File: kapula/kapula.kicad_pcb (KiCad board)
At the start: 4 copper layers, 50 x 59 mm, 163 parts, among them J1 Conn_02x10_Odd_Even, J12 U.FL, J13 U.FL, J3 Conn_02x10_Odd_Even, J4 Conn_ARM_JTAG_SWD_10, J5 U.FL, J9 U.FL, Q1 AO3401A, Q2 AO3401A, Q3 AO3400A, Q4 BSS84, Q5 AO3400A, Q6 AO3400A, T1 BW21S7511A01TF, T2 BW21S7511A01TF, T3 BW21S7511A01TF, T4 BW21S7511A01TF, U1 XC6206P332MR, U2 TP4054, U3 DW01+G, U5 EFR32FG14P233F256GM48-B, U6 XA213-G4J, X1 DSB221SDN, Y1 32768 Hz

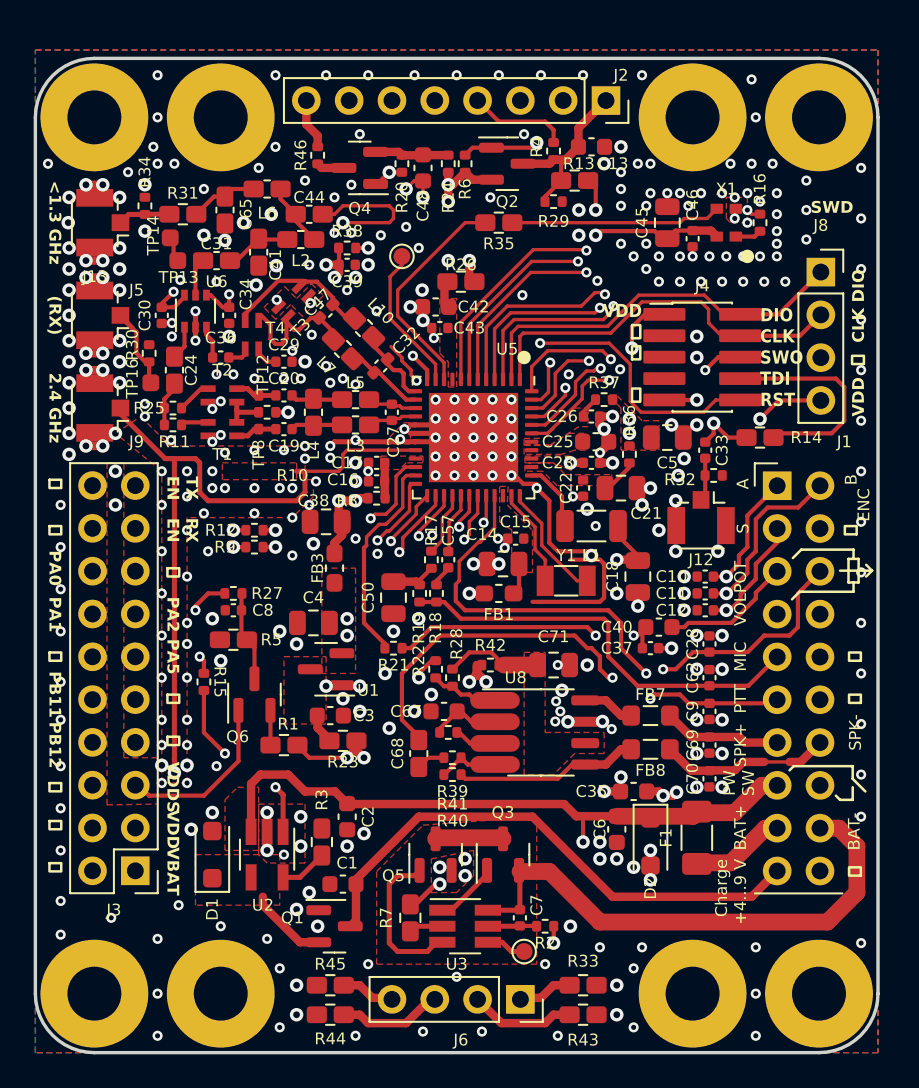
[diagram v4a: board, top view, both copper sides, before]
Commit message: PCB: Add tooling holes
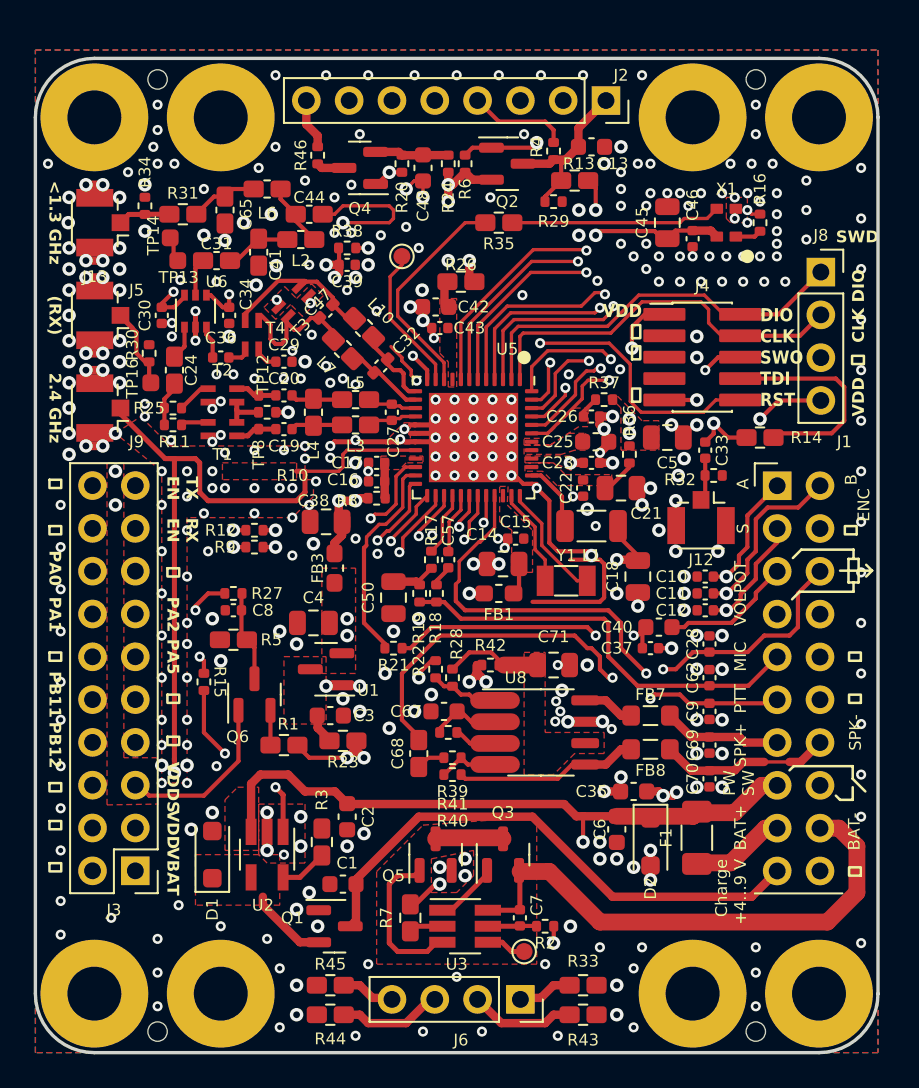
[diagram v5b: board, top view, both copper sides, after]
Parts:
- added H10: ~, kapula:ToolingHole, F.Cu at (142.8, 58.8)
- added H11: ~, kapula:ToolingHole, F.Cu at (107.2, 115.2)
- added H12: ~, kapula:ToolingHole, F.Cu at (142.8, 115.2)
- added H9: ~, kapula:ToolingHole, F.Cu at (107.2, 58.8)
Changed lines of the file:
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@@
     (property "ki_keywords" "connector")
     (attr through_hole)
-    (fp_text reference "J8" (at 0 -2.77 unlocked) (layer "F.SilkS")
+    (fp_text reference "J8" (at 0 -2.18 unlocked) (layer "F.SilkS")
         (effects (font (size 0.7 0.7) (thickness 0.15)))
     )
@@
       (net 82 "Net-(C20-Pad1)") (pinfunction "1") (pintype "passive"))
   )
+  (footprint "kapula:ToolingHole" (layer "F.Cu")
+    (at 142.75 58.75)
+    (property "Sheetfile" "kapula.kicad_sch")
+    (property "Sheetname" "")
+    (property "ki_description" "Mounting Hole without connection")
+    (property "ki_keywords" "mounting hole")
+    (attr through_hole)
+    (fp_text reference "H10" (at 0 0.5) (layer "F.SilkS") hide
+        (effects (font (size 1 1) (thickness 0.15)))
+    )
+    (fp_text value "~" (at 0 -0.5) (layer "F.Fab")
+        (effects (font (size 1 1) (thickness 0.15)))
+    )
+    (pad "" np_thru_hole circle (at 0 0) (size 1.752 1.752) (drill 1.152) (layers "*.Mask")
+      (solder_mask_margin 0.3) (clearance 0.3) (zone_connect 0))
+  )
   (footprint "kapula:R_0402_to_0603_HandSolder" (layer "F.Cu")
     (at 143 80)
@@
     )
   )
+  (footprint "kapula:ToolingHole" (layer "F.Cu")
+    (at 107.25 58.75)
+    (property "Sheetfile" "kapula.kicad_sch")
+    (property "Sheetname" "")
+    (property "ki_description" "Mounting Hole without connection")
+    (property "ki_keywords" "mounting hole")
+    (attr through_hole)
+    (fp_text reference "H9" (at 0 0.5) (layer "F.SilkS") hide
+        (effects (font (size 1 1) (thickness 0.15)))
+    )
+    (fp_text value "~" (at 0 -0.5) (layer "F.Fab")
+        (effects (font (size 1 1) (thickness 0.15)))
+    )
+    (pad "" np_thru_hole circle (at 0 0) (size 1.752 1.752) (drill 1.152) (layers "*.Mask")
+      (solder_mask_margin 0.3) (clearance 0.3) (zone_connect 0))
+  )
   (footprint "Resistor_SMD:R_0402_1005Metric" (layer "F.Cu")
     (at 130.75 66 180)
@@
     )
   )
+  (footprint "kapula:ToolingHole" (layer "F.Cu")
+    (at 107.25 115.25)
+    (property "Sheetfile" "kapula.kicad_sch")
+    (property "Sheetname" "")
+    (property "ki_description" "Mounting Hole without connection")
+    (property "ki_keywords" "mounting hole")
+    (attr through_hole)
+    (fp_text reference "H11" (at 0 0.5) (layer "F.SilkS") hide
+        (effects (font (size 1 1) (thickness 0.15)))
+    )
+    (fp_text value "~" (at 0 -0.5) (layer "F.Fab")
+        (effects (font (size 1 1) (thickness 0.15)))
+    )
+    (pad "" np_thru_hole circle (at 0 0) (size 1.752 1.752) (drill 1.152) (layers "*.Mask")
+      (solder_mask_margin 0.3) (clearance 0.3) (zone_connect 0))
+  )
   (footprint "Connector_PinHeader_2.54mm:PinHeader_2x10_P2.54mm_Vertical" (layer "F.Cu")
     (at 144.02 82.86)
@@
       (net 83 "Net-(C29-Pad2)") (pinfunction "4") (pintype "passive"))
   )
+  (footprint "kapula:ToolingHole" (layer "F.Cu")
+    (at 142.75 115.25)
+    (property "Sheetfile" "kapula.kicad_sch")
+    (property "Sheetname" "")
+    (property "ki_description" "Mounting Hole without connection")
+    (property "ki_keywords" "mounting hole")
+    (attr through_hole)
+    (fp_text reference "H12" (at 0 0.5) (layer "F.SilkS") hide
+        (effects (font (size 1 1) (thickness 0.15)))
+    )
+    (fp_text value "~" (at 0 -0.5) (layer "F.Fab")
+        (effects (font (size 1 1) (thickness 0.15)))
+    )
+    (pad "" np_thru_hole circle (at 0 0) (size 1.752 1.752) (drill 1.152) (layers "*.Mask")
+      (solder_mask_margin 0.3) (clearance 0.3) (zone_connect 0))
+  )
   (footprint "Resistor_SMD:R_0402_1005Metric" (layer "F.Cu")
     (at 133.75 77.75 180)
@@
     (effects (font (size 0.7 0.7) (thickness 0.15)) (justify right bottom mirror))
   )
-  (gr_text "SWD" (at 146 66.75) (layer "F.SilkS")
+  (gr_text "SWD" (at 147.5 68.5) (layer "F.SilkS")
     (effects (font (size 0.7 0.7) (thickness 0.15) bold) (justify left bottom))
   )
@@
   (via (at 138.5 81.25) (size 0.8) (drill 0.4) (layers "F.Cu" "B.Cu") (free) (net 2))
   (via (at 134.25 78.75) (size 0.8) (drill 0.4) (layers "F.Cu" "B.Cu") (net 2))
-  (via (at 107.25 58.5) (size 0.6) (drill 0.3) (layers "F.Cu" "B.Cu") (free) (net 2))
+  (via (at 107.25 60.25) (size 0.6) (drill 0.3) (layers "F.Cu" "B.Cu") (free) (net 2))
   (via (at 149 67) (size 0.6) (drill 0.3) (layers "F.Cu" "B.Cu") (free) (net 2))
   (via (at 105 74.25) (size 0.8) (drill 0.4) (layers "F.Cu" "B.Cu") (free) (net 2))
@@
   (via (at 142.5 63.75) (size 0.6) (drill 0.3) (layers "F.Cu" "B.Cu") (free) (net 2))
   (via (at 119.5 103.5) (size 0.8) (drill 0.4) (layers "F.Cu" "B.Cu") (free) (net 2))
+  (via (at 142.75 111.75) (size 0.6) (drill 0.3) (layers "F.Cu" "B.Cu") (free) (net 2))
   (via (at 106.5 78.75) (size 0.6) (drill 0.3) (layers "F.Cu" "B.Cu") (free) (net 2))
   (via (at 102 78.25) (size 0.8) (drill 0.4) (layers "F.Cu" "B.Cu") (free) (net 2))
@@
   (via (at 125 112) (size 0.6) (drill 0.3) (layers "F.Cu" "B.Cu") (free) (net 2))
   (via (at 104 75) (size 0.8) (drill 0.4) (layers "F.Cu" "B.Cu") (free) (net 2))
-  (via (at 142.75 115.5) (size 0.6) (drill 0.3) (layers "F.Cu" "B.Cu") (free) (net 2))
   (via (at 118.75 65) (size 0.6) (drill 0.3) (layers "F.Cu" "B.Cu") (free) (net 2))
   (via (at 124 106.5) (size 0.8) (drill 0.4) (layers "F.Cu" "B.Cu") (net 2))
@@
   (via (at 122 67.5) (size 0.6) (drill 0.3) (layers "F.Cu" "B.Cu") (free) (net 2))
   (via (at 123.55 85.8) (size 0.6) (drill 0.3) (layers "F.Cu" "B.Cu") (free) (net 2))
-  (via (at 107.25 113) (size 0.6) (drill 0.3) (layers "F.Cu" "B.Cu") (free) (net 2))
+  (via (at 107.25 111.75) (size 0.6) (drill 0.3) (layers "F.Cu" "B.Cu") (free) (net 2))
   (via (at 117.75 67.85) (size 0.6) (drill 0.3) (layers "F.Cu" "B.Cu") (free) (net 2))
   (via (at 140.75 70.75) (size 0.6) (drill 0.3) (layers "F.Cu" "B.Cu") (free) (net 2))
@@
   (via (at 119.75 58.5) (size 0.6) (drill 0.3) (layers "F.Cu" "B.Cu") (net 2))
   (via (at 139.25 100.75) (size 0.8) (drill 0.4) (layers "F.Cu" "B.Cu") (free) (net 2))
-  (via (at 107.25 61) (size 0.6) (drill 0.3) (layers "F.Cu" "B.Cu") (free) (net 2))
+  (via (at 107.25 61.75) (size 0.6) (drill 0.3) (layers "F.Cu" "B.Cu") (free) (net 2))
   (via (at 117.25 94.75) (size 0.8) (drill 0.4) (layers "F.Cu" "B.Cu") (free) (net 2))
   (via (at 127.125 77.75) (size 0.6) (drill 0.3) (layers "F.Cu" "B.Cu") (net 2))
@@
   (via (at 109 96.75) (size 0.6) (drill 0.3) (layers "F.Cu" "B.Cu") (free) (net 2))
   (via (at 138.25 70.75) (size 0.6) (drill 0.3) (layers "F.Cu" "B.Cu") (free) (net 2))
-  (via (at 142.75 61) (size 0.6) (drill 0.3) (layers "F.Cu" "B.Cu") (free) (net 2))
+  (via (at 142.75 62) (size 0.6) (drill 0.3) (layers "F.Cu" "B.Cu") (free) (net 2))
   (via (at 125.5 105) (size 0.8) (drill 0.4) (layers "F.Cu" "B.Cu") (net 2))
   (via (at 124.875 82.25) (size 0.6) (drill 0.3) (layers "F.Cu" "B.Cu") (net 2))
@@
   (via (at 149 110) (size 0.6) (drill 0.3) (layers "F.Cu" "B.Cu") (free) (net 2))
   (via (at 102 75.5) (size 0.8) (drill 0.4) (layers "F.Cu" "B.Cu") (free) (net 2))
-  (via (at 142.75 113) (size 0.6) (drill 0.3) (layers "F.Cu" "B.Cu") (free) (net 2))
+  (via (at 142.75 113.75) (size 0.6) (drill 0.3) (layers "F.Cu" "B.Cu") (free) (net 2))
   (via (at 143.75 63.75) (size 0.6) (drill 0.3) (layers "F.Cu" "B.Cu") (free) (net 2))
   (via (at 119 76.85) (size 0.6) (drill 0.3) (layers "F.Cu" "B.Cu") (free) (net 2))
@@
   (via (at 105 70) (size 0.8) (drill 0.4) (layers "F.Cu" "B.Cu") (free) (net 2))
   (via (at 102 72.75) (size 0.8) (drill 0.4) (layers "F.Cu" "B.Cu") (free) (net 2))
-  (via (at 142.5 58.75) (size 0.6) (drill 0.3) (layers "F.Cu" "B.Cu") (free) (net 2))
+  (via (at 142.75 60.25) (size 0.6) (drill 0.3) (layers "F.Cu" "B.Cu") (free) (net 2))
   (via (at 139.25 79.25) (size 0.8) (drill 0.4) (layers "F.Cu" "B.Cu") (free) (net 2))
   (via (at 136.5 106.25) (size 0.8) (drill 0.4) (layers "F.Cu" "B.Cu") (free) (net 2))
@@
   (via (at 102 65.75) (size 0.8) (drill 0.4) (layers "F.Cu" "B.Cu") (free) (net 2))
   (via (at 142.25 67.25) (size 0.6) (drill 0.3) (layers "F.Cu" "B.Cu") (free) (net 2))
-  (via (at 107.25 115.5) (size 0.6) (drill 0.3) (layers "F.Cu" "B.Cu") (free) (net 2))
+  (via (at 107.25 113.75) (size 0.6) (drill 0.3) (layers "F.Cu" "B.Cu") (free) (net 2))
   (via (at 143 66) (size 0.6) (drill 0.3) (layers "F.Cu" "B.Cu") (free) (net 2))
   (via (at 142.25 66.5) (size 0.6) (drill 0.3) (layers "F.Cu" "B.Cu") (free) (net 2))

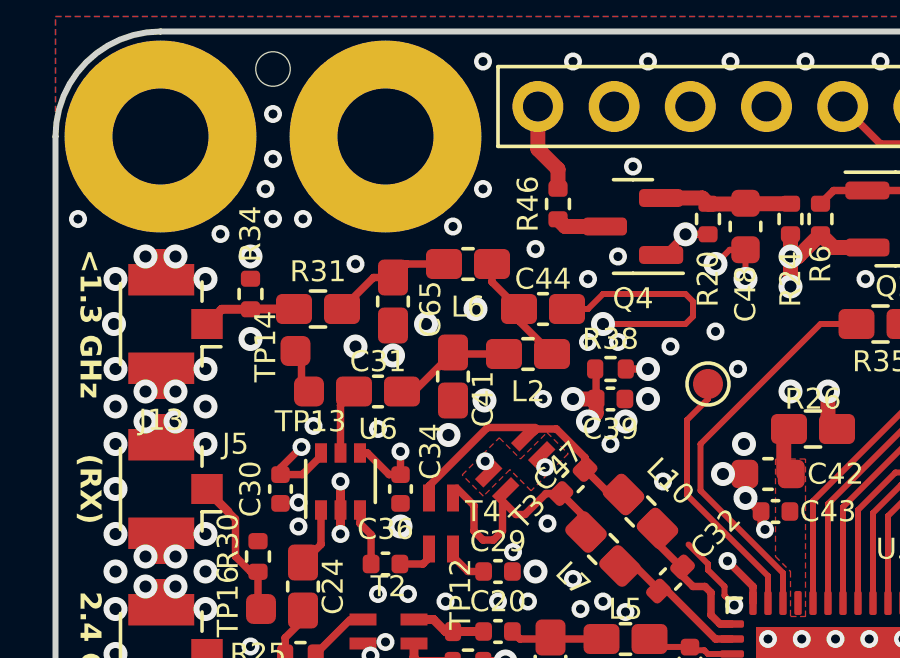
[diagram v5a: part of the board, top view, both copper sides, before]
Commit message: PCB: Move lowpass components more away from display signals
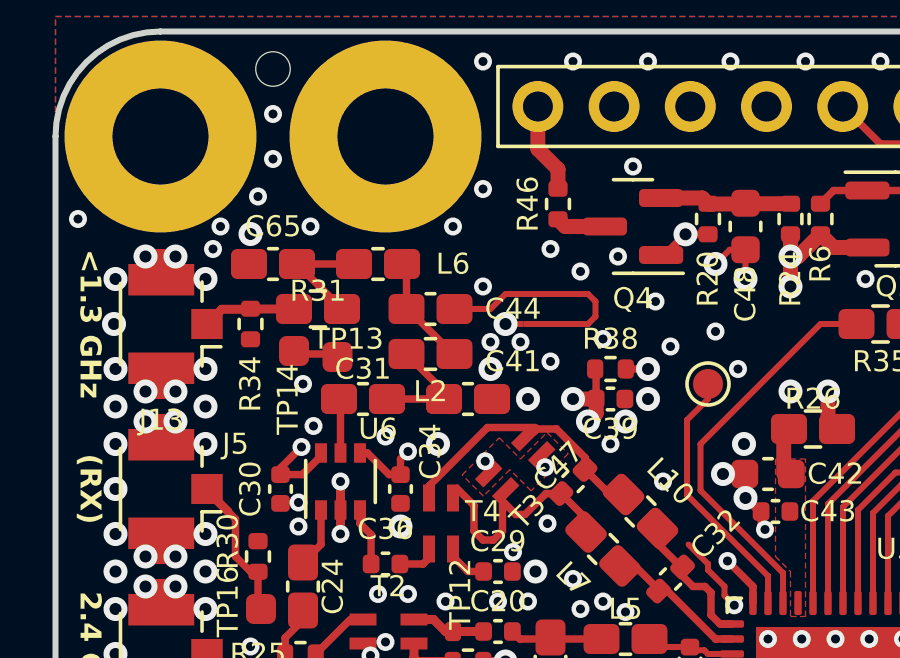
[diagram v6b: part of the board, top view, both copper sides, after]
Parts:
- moved C65 4.19 mm to (107.2, 65.2), turned to 180 degrees
- moved C44 3.75 mm to (112.5, 66.8)
- moved L2 3.25 mm to (112.5, 68.2)
- moved NT2 3.25 mm to (115.5, 67.2)
- moved L6 3.00 mm to (110.8, 65.2)
- moved TP13 1.49 mm to (109.4, 68.3)
- moved R34 1.00 mm to (106.5, 67.2), turned to 90 degrees
- moved C41 0.90 mm to (113.8, 69.8), turned to 0 degrees
- moved C31 0.56 mm to (110.2, 69.8)
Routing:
- net GND: track 68.7 -> 72.3 mm, vias 389 -> 388
- net Net-(C44-Pad2): track 7.41 -> 7.91 mm
